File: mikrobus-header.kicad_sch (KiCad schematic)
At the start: 0 parts

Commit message: mostly done with schematic of mikrobus board
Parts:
- added J3, J4: Conn_01x08_Pin, Connector_PinHeader_2.54mm:PinHeader_1x08_P2.54mm_Vertical, symbol Connector:Conn_01x08_Pin
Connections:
- new net +3V3: J4.7 (Pin_7)
- new net +5V: J3.7 (Pin_7)
- new net BIT: J3.1 (Pin_1)
- new net CNT: J4.5 (Pin_5)
- new net DI: J4.1 (Pin_1)
- new net DO: J3.2 (Pin_2)
- new net GND: J3.8 (Pin_8), J4.8 (Pin_8)
- new net SCL: J3.5 (Pin_5)
- new net SDA: J3.6 (Pin_6)
- new net TS: J4.6 (Pin_6)
- new net WRD: J4.2 (Pin_2)

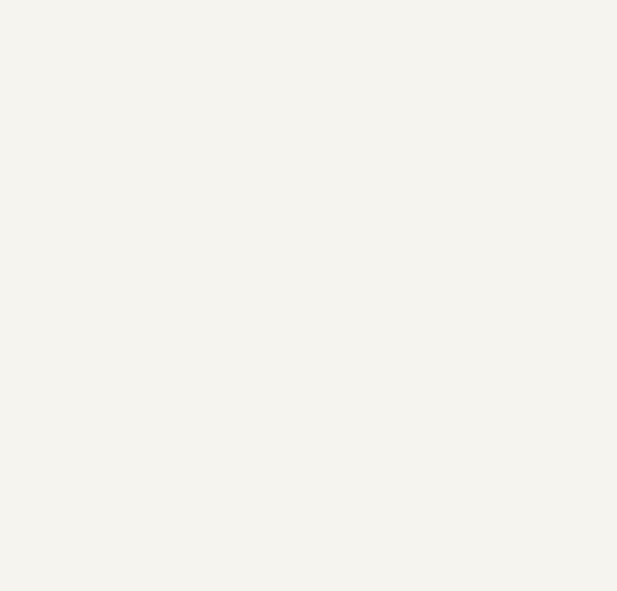
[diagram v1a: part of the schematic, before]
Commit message: add 1-wire eeprom and a bit more
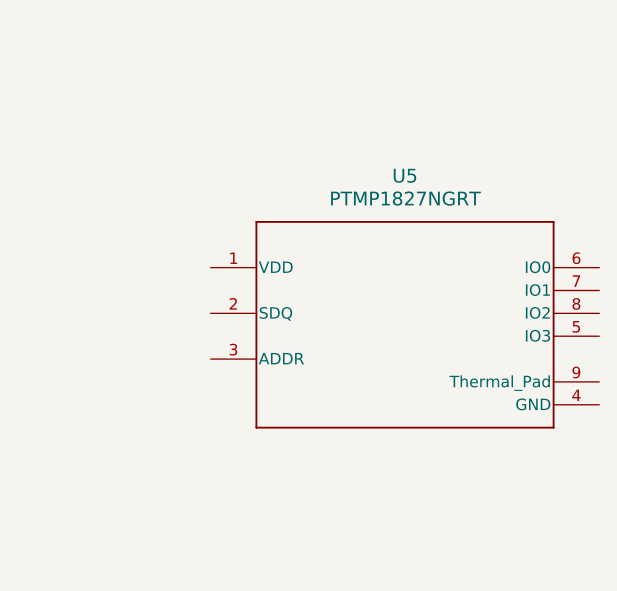
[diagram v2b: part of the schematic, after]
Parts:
- added U5: PTMP1827NGRT, Library:NGR0008B-IPC_A, symbol Library:PTMP1827NGRT
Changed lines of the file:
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@@
+	)
+	(symbol
+		(lib_id "Library:PTMP1827NGRT")
+		(at 179.07 54.61 0)
+		(unit 1)
+		(exclude_from_sim no)
+		(in_bom yes)
+		(on_board yes)
+		(dnp no)
+		(fields_autoplaced yes)
+		(property "Reference" "U5"
+			(at 200.66 44.45 0)
+			(effects
+				(font
+					(size 1.524 1.524)
+				)
+			)
+		)
+		(property "Value" "PTMP1827NGRT"
+			(at 200.66 46.99 0)
+			(effects
+				(font
+					(size 1.524 1.524)
+				)
+			)
+		)
+		(property "Footprint" "Library:NGR0008B-IPC_A"
+			(at 179.07 54.61 0)
+			(effects
+				(font
+					(size 1.27 1.27)
+					(italic yes)
+				)
+				(hide yes)
+			)
+		)
+		(property "Datasheet" "PTMP1827NGRT"
+			(at 179.07 54.61 0)
+			(effects
+				(font
+					(size 1.27 1.27)
+					(italic yes)
+				)
+				(hide yes)
+			)
+		)
+		(property "Description" ""
+			(at 179.07 54.61 0)
+			(effects
+				(font
+					(size 1.27 1.27)
+				)
+				(hide yes)
+			)
+		)
+		(pin "5"
+		)
+		(pin "3"
+		)
+		(pin "7"
+		)
+		(pin "6"
+		)
+		(pin "1"
+		)
+		(pin "4"
+		)
+		(pin "2"
+		)
+		(pin "8"
+		)
+		(pin "9"
+		)
+		(instances
+			(project ""
+				(path "/df100556-b288-4cb1-b69f-c0734132cb90/8a24c5c7-3a1e-4ea3-b8af-25956c30237e"
+					(reference "U5")
+					(unit 1)
+				)
+			)
+		)
 	)
 	(symbol

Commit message: add clickid
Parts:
- added U7: 74LVC1G3157, symbol 74xGxx:74LVC1G3157
- U5: value PTMP1827NGRT -> TMP1827NGRR
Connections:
- net WRD: now also U7.6
- net at J4.3 (Pin_3): now also U7.4
- net at U5.2 (SDQ): now also U7.3
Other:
- note added: "AN"
- note added: "CS"
- note added: "INT"
- note added: "PICO"
- note added: "POCI"
- note added: "PWM"
- note added: "RST"
- note added: "RX"
- note added: "SCK"
- note added: "TX"

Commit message: Resolve #5: Finished up ClickId Ciruit
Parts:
- removed U7: 74LVC1G3157, symbol 74xGxx:74LVC1G3157
- added C23: 0.1uF, Capacitor_SMD:C_0603_1608Metric, symbol Device:C
- added R15: 2.2K, Resistor_SMD:R_0603_1608Metric, symbol Device:R
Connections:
- net +3V3: now also U5.1 (VDD), C23.1, R15.1
- net GND: now also U5.3 (ADDR), U5.4 (GND), U5.5 (IO3), U5.6 (IO0), U5.7 (IO1), U5.8 (IO2), U5.9 (Thermal_Pad), C23.2
- net at U5.2 (SDQ): now also J4.3 (Pin_3), R15.2

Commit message: add extra labels to MB and title. specify project in CI file and update to Kicad 8.0.8
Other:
- note added: "3V3"
- note added: "5V"
- note added: "GND"
- note added: "SCL"
- note added: "SDA"
- company: (none) -> JKEmbedded, LLC
- title: (none) -> JKEmbedded Audio Board
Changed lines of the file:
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@@
 	(generator_version "8.0")
 	(paper "USLetter")
+	(title_block
+		(title "JKEmbedded Audio Board")
+		(company "JKEmbedded, LLC")
+	)
 	(junction
 		(at 156.21 59.69)
@@
 		)
 	)
+	(text "5V"
+		(exclude_from_sim no)
+		(at 67.056 53.848 0)
+		(effects
+			(font
+				(size 1.27 1.27)
+			)
+		)
+	)
 	(text "RST"
 		(exclude_from_sim no)
@@
 		)
 	)
+	(text "3V3"
+		(exclude_from_sim no)
+		(at 68.072 108.458 0)
+		(effects
+			(font
+				(size 1.27 1.27)
+			)
+		)
+	)
 	(text "SCK"
 		(exclude_from_sim no)
@@
 		)
 	)
+	(text "SDA"
+		(exclude_from_sim no)
+		(at 66.802 51.308 0)
+		(effects
+			(font
+				(size 1.27 1.27)
+			)
+		)
+	)
+	(text "GND"
+		(exclude_from_sim no)
+		(at 68.326 110.998 0)
+		(effects
+			(font
+				(size 1.27 1.27)
+			)
+		)
+	)
 	(text "AN"
 		(exclude_from_sim no)
@@
 		)
 	)
+	(text "SCL"
+		(exclude_from_sim no)
+		(at 66.802 48.768 0)
+		(effects
+			(font
+				(size 1.27 1.27)
+			)
+		)
+	)
 	(text "INT"
 		(exclude_from_sim no)
@@
 		(effects
 			(font
+				(size 1.27 1.27)
+			)
+		)
+	)
+	(text "GND"
+		(exclude_from_sim no)
+		(at 67.31 56.642 0)
+		(effects
+			(font

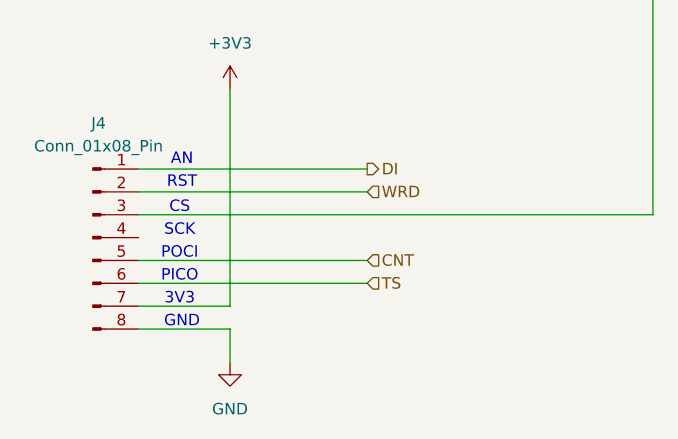
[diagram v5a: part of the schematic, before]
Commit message: Resolved #2: Matched 4 clock outputs to expected by DEP
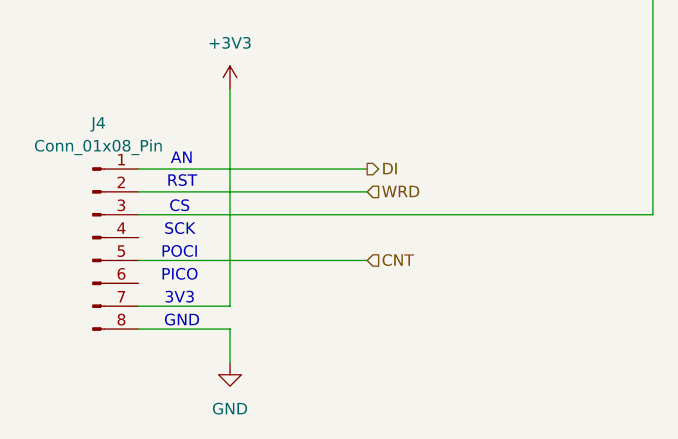
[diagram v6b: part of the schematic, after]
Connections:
- net TS: no longer names the net of J4.6 (Pin_6)
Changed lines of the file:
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@@
-	(wire
-		(pts
-			(xy 63.5 106.68) (xy 88.9 106.68)
-		)
-		(stroke
-			(width 0)
-			(type default)
-		)
-	)
 	(wire
 		(pts
@@
 		(effects
 			(font
-				(size 1.27 1.27)
-			)
-			(justify left)
-		)
-	)
-	(hierarchical_label "TS"
-		(shape input)
-		(at 88.9 106.68 0)
-		(effects
-			(font

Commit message: Add TS
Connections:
- net TS: now reaches J4.6 (Pin_6)
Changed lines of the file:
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@@
+	(wire
+		(pts
+			(xy 63.5 106.68) (xy 88.9 106.68)
+		)
+		(stroke
+			(width 0)
+			(type default)
+		)
+	)
 	(wire
 		(pts
@@
 			(width 0)
 			(type default)
+		)
+	)
+	(text_box "Single Wire EEPROM for ClickID"
+		(exclude_from_sim no)
+		(at 217.17 31.75 0)
+		(size 21.59 12.7)
+		(stroke
+			(width 0)
+			(type default)
+		)
+		(fill
+			(type none)
+		)
+		(effects
+			(font
+				(size 1.27 1.27)
+			)
+			(justify left top)
 		)
 	)
@@
 		(effects
 			(font
+				(size 1.27 1.27)
+			)
+			(justify left)
+		)
+	)
+	(hierarchical_label "TS"
+		(shape input)
+		(at 88.9 106.68 0)
+		(effects
+			(font

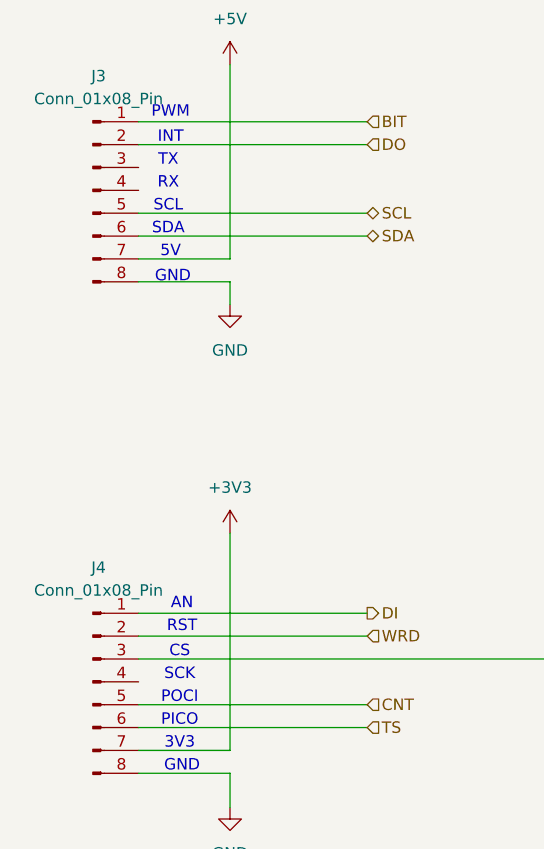
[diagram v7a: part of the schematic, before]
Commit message: worked through ERCs and updated PCB components
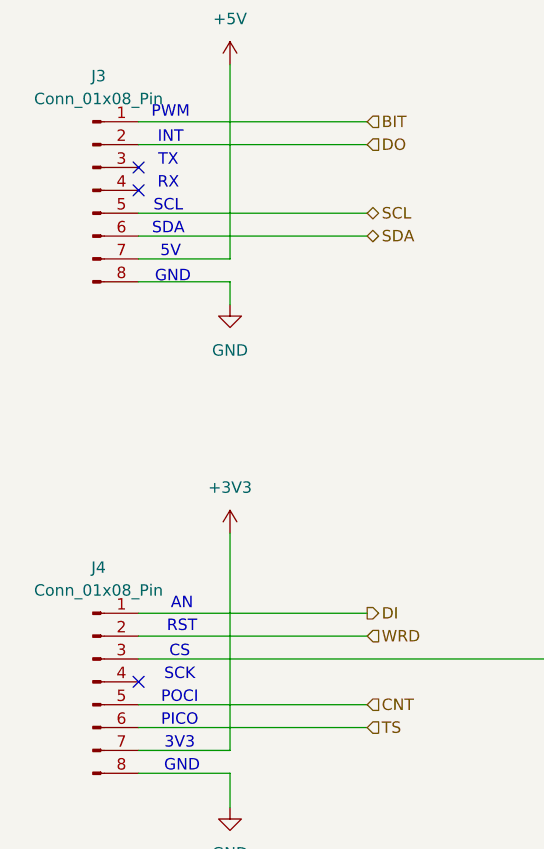
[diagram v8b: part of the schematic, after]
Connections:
- no-connect marks 0 -> 3
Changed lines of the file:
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@@
 		(color 0 0 0 0)
+	)
+	(no_connect
+		(at 63.5 46.99)
+	)
+	(no_connect
+		(at 63.5 44.45)
+	)
+	(no_connect
+		(at 63.5 101.6)
 	)
 	(wire
